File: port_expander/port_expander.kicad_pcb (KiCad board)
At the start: 2 copper layers, 104 x 71 mm, 22 parts, among them J0 Conn_02x08_Male, J1 Conn_02x08_Male, J10 Conn_01x05_Male, J2 Conn_02x08_Male, J3 Conn_02x08_Male, J4 Conn_02x08_Male, J5 Conn_02x08_Male, J6 Conn_02x08_Male, J7 Conn_02x08_Male, J8 Conn_02x08_Male, J9 Conn_02x08_Male, U1 74LS30

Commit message: compact port expander layout
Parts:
- removed H1, H2, H3: MountingHole_3.2mm_M3_Pad, MountingHole:MountingHole_3.2mm_M3_Pad
- removed LOGO: KiCad-Logo2_5mm_SilkScreen, Symbol:KiCad-Logo2_5mm_SilkScreen
- removed OSH: OSHW-Logo2_7.3x6mm_SilkScreen, Symbol:OSHW-Logo2_7.3x6mm_SilkScreen
- added L0: KiCad-Logo_5mm_SilkScreen, Symbol:KiCad-Logo_5mm_SilkScreen, B.Cu at (150.2, 66.9)
- added MH0: MountingHole_3.2mm_M3, MountingHole:MountingHole_3.2mm_M3, F.Cu at (26.5, 59.5)
- added MH1: MountingHole_3.2mm_M3, MountingHole:MountingHole_3.2mm_M3, F.Cu at (150.0, 59.5)
- added MH2: MountingHole_3.2mm_M3, MountingHole:MountingHole_3.2mm_M3, F.Cu at (254.5, 59.5)
- added REF**: OSHW-Logo_5.7x6mm_SilkScreen, Symbol:OSHW-Logo_5.7x6mm_SilkScreen, B.Cu at (240.7, 68.7)
- J0, J1, J2, J3, J4, J5, J6, J7, J8, J9: footprint Connector_PinHeader_2.54mm:PinHeader_2x08_P2.54mm_Vertical -> Connector_PinHeader_2.54mm:PinHeader_2x08_P2.54mm_Horizontal
- U1: value 74LS30 -> 74HC32
- moved PE4 99.6 mm to (228.0, 55.6), turned to 270 degrees
- moved PE3 97.1 mm to (190.5, 55.6), turned to 270 degrees
- moved J9 89.6 mm to (236.5, 71.8), turned to 270 degrees
- moved U1 88.6 mm to (248.0, 55.6), turned to 270 degrees
- moved J1 85.5 mm to (64.3, 71.8), turned to 270 degrees
- moved J7 80.8 mm to (193.4, 71.8), turned to 270 degrees
- moved J0 76.4 mm to (42.8, 71.8), turned to 270 degrees
- moved J8 75.9 mm to (215.0, 71.8), turned to 270 degrees
- moved J3 75.2 mm to (107.3, 71.8), turned to 270 degrees
- moved J6 73.0 mm to (171.9, 71.8), turned to 270 degrees
- moved PE0 67.8 mm to (66.5, 55.6), turned to 270 degrees
- moved J2 65.4 mm to (85.8, 71.8), turned to 270 degrees
- moved J5 65.3 mm to (150.4, 71.8), turned to 270 degrees
- moved PE1 62.3 mm to (104.5, 55.6), turned to 270 degrees
- moved PE2 57.0 mm to (142.5, 55.6), turned to 270 degrees
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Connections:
- J0 pad 1: GND -> /E0B0
- J0 pad 10: Net-(J0-Pad10) -> GND
- J0 pad 11: GND -> /E0B5
- J0 pad 12: Net-(J0-Pad12) -> GND
- J0 pad 13: GND -> /E0B6
- J0 pad 14: Net-(J0-Pad14) -> GND
- J0 pad 15: GND -> /E0B7
- J0 pad 16: Net-(J0-Pad16) -> GND
- J0 pad 2: Net-(J0-Pad2) -> GND
- J0 pad 3: GND -> /E0B1
- J0 pad 4: Net-(J0-Pad4) -> GND
- J0 pad 5: GND -> /E0B2
- J0 pad 6: Net-(J0-Pad6) -> GND
- J0 pad 7: GND -> /E0B3
- J0 pad 8: Net-(J0-Pad8) -> GND
- J0 pad 9: GND -> /E0B4
- J1 pad 1: GND -> /E0A7
- J1 pad 10: Net-(J1-Pad10) -> GND
- J1 pad 11: GND -> /E0A2
- J1 pad 12: Net-(J1-Pad12) -> GND
- J1 pad 13: GND -> /E0A1
- J1 pad 14: Net-(J1-Pad14) -> GND
- J1 pad 15: GND -> /E0A0
- J1 pad 16: Net-(J1-Pad16) -> GND
- J1 pad 2: Net-(J1-Pad2) -> GND
- J1 pad 3: GND -> /E0A6
- J1 pad 4: Net-(J1-Pad4) -> GND
- J1 pad 5: GND -> /E0A5
- J1 pad 6: Net-(J1-Pad6) -> GND
- J1 pad 7: GND -> /E0A4
- J1 pad 8: Net-(J1-Pad8) -> GND
- J1 pad 9: GND -> /E0A3
- J2 pad 1: GND -> /E1B0
- J2 pad 10: Net-(J2-Pad10) -> GND
- J2 pad 11: GND -> /E1B5
- J2 pad 12: Net-(J2-Pad12) -> GND
- J2 pad 13: GND -> /E1B6
- J2 pad 14: Net-(J2-Pad14) -> GND
- J2 pad 15: GND -> /E1B7
- J2 pad 16: Net-(J2-Pad16) -> GND
- J2 pad 2: Net-(J2-Pad2) -> GND
- J2 pad 3: GND -> /E1B1
- J2 pad 4: Net-(J2-Pad4) -> GND
- J2 pad 5: GND -> /E1B2
- J2 pad 6: Net-(J2-Pad6) -> GND
- J2 pad 7: GND -> /E1B3
- J2 pad 8: Net-(J2-Pad8) -> GND
- J2 pad 9: GND -> /E1B4
- J3 pad 1: GND -> /E1A7
- J3 pad 10: Net-(J3-Pad10) -> GND
- J3 pad 11: GND -> /E1A2
- J3 pad 12: Net-(J3-Pad12) -> GND
- J3 pad 13: GND -> /E1A1
- J3 pad 14: Net-(J3-Pad14) -> GND
- J3 pad 15: GND -> /E1A0
- J3 pad 16: Net-(J3-Pad16) -> GND
- J3 pad 2: Net-(J3-Pad2) -> GND
- J3 pad 3: GND -> /E1A6
- J3 pad 4: Net-(J3-Pad4) -> GND
- J3 pad 5: GND -> /E1A5
- J3 pad 6: Net-(J3-Pad6) -> GND
- J3 pad 7: GND -> /E1A4
- J3 pad 8: Net-(J3-Pad8) -> GND
- J3 pad 9: GND -> /E1A3
- J4 pad 1: GND -> /E2B0
- J4 pad 10: Net-(J4-Pad10) -> GND
- J4 pad 11: GND -> /E2B5
- J4 pad 12: Net-(J4-Pad12) -> GND
- J4 pad 13: GND -> /E2B6
- J4 pad 14: Net-(J4-Pad14) -> GND
- J4 pad 15: GND -> /E2B7
- J4 pad 16: Net-(J4-Pad16) -> GND
- J4 pad 2: Net-(J4-Pad2) -> GND
- J4 pad 3: GND -> /E2B1
- J4 pad 4: Net-(J4-Pad4) -> GND
- J4 pad 5: GND -> /E2B2
- J4 pad 6: Net-(J4-Pad6) -> GND
- J4 pad 7: GND -> /E2B3
- J4 pad 8: Net-(J4-Pad8) -> GND
- J4 pad 9: GND -> /E2B4
- J5 pad 1: GND -> /E2A7
- J5 pad 10: Net-(J5-Pad10) -> GND
- J5 pad 11: GND -> /E2A2
- J5 pad 12: Net-(J5-Pad12) -> GND
- J5 pad 13: GND -> /E2A1
- J5 pad 14: Net-(J5-Pad14) -> GND
- J5 pad 15: GND -> /E2A0
- J5 pad 16: Net-(J5-Pad16) -> GND
- J5 pad 2: Net-(J5-Pad2) -> GND
- J5 pad 3: GND -> /E2A6
- J5 pad 4: Net-(J5-Pad4) -> GND
- J5 pad 5: GND -> /E2A5
- J5 pad 6: Net-(J5-Pad6) -> GND
- J5 pad 7: GND -> /E2A4
- J5 pad 8: Net-(J5-Pad8) -> GND
- J5 pad 9: GND -> /E2A3
- J6 pad 1: GND -> /E3B0
- J6 pad 10: Net-(J6-Pad10) -> GND
- J6 pad 11: GND -> /E3B5
- J6 pad 12: Net-(J6-Pad12) -> GND
- J6 pad 13: GND -> /E3B6
- J6 pad 14: Net-(J6-Pad14) -> GND
- J6 pad 15: GND -> /E3B7
- J6 pad 16: Net-(J6-Pad16) -> GND
- J6 pad 2: Net-(J6-Pad2) -> GND
- J6 pad 3: GND -> /E3B1
- J6 pad 4: Net-(J6-Pad4) -> GND
- J6 pad 5: GND -> /E3B2
- J6 pad 6: Net-(J6-Pad6) -> GND
- J6 pad 7: GND -> /E3B3
- J6 pad 8: Net-(J6-Pad8) -> GND
- J6 pad 9: GND -> /E3B4
- J7 pad 1: GND -> /E3A7
- J7 pad 10: Net-(J7-Pad10) -> GND
- J7 pad 11: GND -> /E3A2
- J7 pad 12: Net-(J7-Pad12) -> GND
- J7 pad 13: GND -> /E3A1
- J7 pad 14: Net-(J7-Pad14) -> GND
- J7 pad 15: GND -> /E3A0
- J7 pad 16: Net-(J7-Pad16) -> GND
- J7 pad 2: Net-(J7-Pad2) -> GND
- J7 pad 3: GND -> /E3A6
- J7 pad 4: Net-(J7-Pad4) -> GND
- J7 pad 5: GND -> /E3A5
- J7 pad 6: Net-(J7-Pad6) -> GND
- J7 pad 7: GND -> /E3A4
- J7 pad 8: Net-(J7-Pad8) -> GND
- J7 pad 9: GND -> /E3A3
- J8 pad 1: GND -> /E4B0
- J8 pad 10: Net-(J8-Pad10) -> GND
- J8 pad 11: GND -> /E4B5
- J8 pad 12: Net-(J8-Pad12) -> GND
- J8 pad 13: GND -> /E4B6
- J8 pad 14: Net-(J8-Pad14) -> GND
- J8 pad 15: GND -> /E4B7
- J8 pad 16: Net-(J8-Pad16) -> GND
- J8 pad 2: Net-(J8-Pad2) -> GND
- J8 pad 3: GND -> /E4B1
- J8 pad 4: Net-(J8-Pad4) -> GND
- J8 pad 5: GND -> /E4B2
- J8 pad 6: Net-(J8-Pad6) -> GND
- J8 pad 7: GND -> /E4B3
- J8 pad 8: Net-(J8-Pad8) -> GND
- J8 pad 9: GND -> /E4B4
- J9 pad 1: GND -> /E4A7
- J9 pad 10: Net-(J9-Pad10) -> GND
- J9 pad 11: GND -> /E4A2
- J9 pad 12: Net-(J9-Pad12) -> GND
- J9 pad 13: GND -> /E4A1
- J9 pad 14: Net-(J9-Pad14) -> GND
- J9 pad 15: GND -> /E4A0
- J9 pad 16: Net-(J9-Pad16) -> GND
- J9 pad 2: Net-(J9-Pad2) -> GND
- J9 pad 3: GND -> /E4A6
- J9 pad 4: Net-(J9-Pad4) -> GND
- J9 pad 5: GND -> /E4A5
- J9 pad 6: Net-(J9-Pad6) -> GND
- J9 pad 7: GND -> /E4A4
- J9 pad 8: Net-(J9-Pad8) -> GND
- J9 pad 9: GND -> /E4A3
- PE0 pad 1: Net-(J0-Pad2) -> /E0B0
- PE0 pad 2: Net-(J0-Pad4) -> /E0B1
- PE0 pad 21: Net-(J1-Pad2) -> /E0A0
- PE0 pad 22: Net-(J1-Pad4) -> /E0A1
- PE0 pad 23: Net-(J1-Pad6) -> /E0A2
- PE0 pad 24: Net-(J1-Pad8) -> /E0A3
- PE0 pad 25: Net-(J1-Pad10) -> /E0A4
- PE0 pad 26: Net-(J1-Pad12) -> /E0A5
- PE0 pad 27: Net-(J1-Pad14) -> /E0A6
- PE0 pad 28: Net-(J1-Pad16) -> /E0A7
- PE0 pad 3: Net-(J0-Pad6) -> /E0B2
- PE0 pad 4: Net-(J0-Pad8) -> /E0B3
- PE0 pad 5: Net-(J0-Pad10) -> /E0B4
- PE0 pad 6: Net-(J0-Pad12) -> /E0B5
- PE0 pad 7: Net-(J0-Pad14) -> /E0B6
- PE0 pad 8: Net-(J0-Pad16) -> /E0B7
- PE1 pad 1: Net-(J2-Pad2) -> /E1B0
- PE1 pad 2: Net-(J2-Pad4) -> /E1B1
- PE1 pad 21: Net-(J3-Pad2) -> /E1A0
- PE1 pad 22: Net-(J3-Pad4) -> /E1A1
- PE1 pad 23: Net-(J3-Pad6) -> /E1A2
- PE1 pad 24: Net-(J3-Pad8) -> /E1A3
- PE1 pad 25: Net-(J3-Pad10) -> /E1A4
- PE1 pad 26: Net-(J3-Pad12) -> /E1A5
- PE1 pad 27: Net-(J3-Pad14) -> /E1A6
- PE1 pad 28: Net-(J3-Pad16) -> /E1A7
- PE1 pad 3: Net-(J2-Pad6) -> /E1B2
- PE1 pad 4: Net-(J2-Pad8) -> /E1B3
- PE1 pad 5: Net-(J2-Pad10) -> /E1B4
- PE1 pad 6: Net-(J2-Pad12) -> /E1B5
- PE1 pad 7: Net-(J2-Pad14) -> /E1B6
- PE1 pad 8: Net-(J2-Pad16) -> /E1B7
- PE2 pad 1: Net-(J4-Pad2) -> /E2B0
- PE2 pad 2: Net-(J4-Pad4) -> /E2B1
- PE2 pad 21: Net-(J5-Pad2) -> /E2A0
- PE2 pad 22: Net-(J5-Pad4) -> /E2A1
- PE2 pad 23: Net-(J5-Pad6) -> /E2A2
- PE2 pad 24: Net-(J5-Pad8) -> /E2A3
- PE2 pad 25: Net-(J5-Pad10) -> /E2A4
- PE2 pad 26: Net-(J5-Pad12) -> /E2A5
- PE2 pad 27: Net-(J5-Pad14) -> /E2A6
- PE2 pad 28: Net-(J5-Pad16) -> /E2A7
- PE2 pad 3: Net-(J4-Pad6) -> /E2B2
- PE2 pad 4: Net-(J4-Pad8) -> /E2B3
- PE2 pad 5: Net-(J4-Pad10) -> /E2B4
- PE2 pad 6: Net-(J4-Pad12) -> /E2B5
- PE2 pad 7: Net-(J4-Pad14) -> /E2B6
- PE2 pad 8: Net-(J4-Pad16) -> /E2B7
- PE3 pad 1: Net-(J6-Pad2) -> /E3B0
- PE3 pad 2: Net-(J6-Pad4) -> /E3B1
- PE3 pad 21: Net-(J7-Pad2) -> /E3A0
- PE3 pad 22: Net-(J7-Pad4) -> /E3A1
- PE3 pad 23: Net-(J7-Pad6) -> /E3A2
- PE3 pad 24: Net-(J7-Pad8) -> /E3A3
- PE3 pad 25: Net-(J7-Pad10) -> /E3A4
- PE3 pad 26: Net-(J7-Pad12) -> /E3A5
- PE3 pad 27: Net-(J7-Pad14) -> /E3A6
- PE3 pad 28: Net-(J7-Pad16) -> /E3A7
- PE3 pad 3: Net-(J6-Pad6) -> /E3B2
- PE3 pad 4: Net-(J6-Pad8) -> /E3B3
- PE3 pad 5: Net-(J6-Pad10) -> /E3B4
- PE3 pad 6: Net-(J6-Pad12) -> /E3B5
- PE3 pad 7: Net-(J6-Pad14) -> /E3B6
- PE3 pad 8: Net-(J6-Pad16) -> /E3B7
- PE4 pad 1: Net-(J8-Pad2) -> /E4B0
- PE4 pad 2: Net-(J8-Pad4) -> /E4B1
- PE4 pad 21: Net-(J9-Pad2) -> /E4A0
- PE4 pad 22: Net-(J9-Pad4) -> /E4A1
- PE4 pad 23: Net-(J9-Pad6) -> /E4A2
- PE4 pad 24: Net-(J9-Pad8) -> /E4A3
- PE4 pad 25: Net-(J9-Pad10) -> /E4A4
- PE4 pad 26: Net-(J9-Pad12) -> /E4A5
- PE4 pad 27: Net-(J9-Pad14) -> /E4A6
- PE4 pad 28: Net-(J9-Pad16) -> /E4A7
- PE4 pad 3: Net-(J8-Pad6) -> /E4B2
- PE4 pad 4: Net-(J8-Pad8) -> /E4B3
- PE4 pad 5: Net-(J8-Pad10) -> /E4B4
- PE4 pad 6: Net-(J8-Pad12) -> /E4B5
- PE4 pad 7: Net-(J8-Pad14) -> /E4B6
- PE4 pad 8: Net-(J8-Pad16) -> /E4B7
- U1 pad 10: (no net) -> /INT3
- U1 pad 11: +3V3 -> /INT
- U1 pad 12: +3V3 -> Net-(U1-Pad12)
- U1 pad 13: (no net) -> /INT4
- U1 pad 3: /INT2 -> Net-(U1-Pad3)
- U1 pad 4: /INT3 -> Net-(U1-Pad3)
- U1 pad 5: /INT4 -> /INT2
- U1 pad 6: +3V3 -> Net-(U1-Pad6)
- U1 pad 8: /INT -> Net-(U1-Pad12)
- U1 pad 9: (no net) -> Net-(U1-Pad6)
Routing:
- net /SCK: track 99.2 -> 232.6 mm
- net /INT1: track 43.7 -> 175.6 mm
- net /INT0: track 75.9 -> 207.7 mm
- net /SDA: track 107.0 -> 235.3 mm
- net +3V3: track 179.5 -> 281.6 mm
- net /INT2: track 27.1 -> 122.0 mm
- net /E3B1: track 0.00 -> 89.5 mm
- net /E3B2: track 0.00 -> 55.6 mm
- net /E0B1: track 0.00 -> 47.9 mm
- net /E3B0: track 0.00 -> 47.9 mm
- net /E0B2: track 0.00 -> 44.3 mm
- net /E0B3: track 0.00 -> 41.5 mm
- net /E3B3: track 0.00 -> 37.9 mm
- net /E1B0: track 0.00 -> 36.4 mm
- net /E0B5: track 0.00 -> 35.7 mm
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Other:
- board size 104 x 71 mm -> 239 x 26 mm
- net class Power: clearance 0.4 -> 0.3; trace_width 0.5 -> 0.3; via_dia 1.6 -> 1; via_drill 0.8 -> 0.5
- board text added: "Port Expander 80 GPIOs I2C"
- board text removed: "Port Expander Interrupt 80 GPIOs I2C"

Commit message: port expander with MCU
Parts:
- added J11: Power_Jack, Connector_PinHeader_2.54mm:PinHeader_1x02_P2.54mm_Vertical, F.Cu at (296.0, 49.0)
- added MC1: ESP32_DevKitC, esp32_driver:ESP32_DevKitC, F.Cu at (345.0, 79.2)
- J10: value Conn_01x05_Male -> OLED_Display; footprint Connector_PinHeader_2.54mm:PinHeader_1x05_P2.54mm_Vertical -> Connector_PinHeader_2.54mm:PinHeader_1x04_P2.54mm_Vertical
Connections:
- J10 pad 3: /SDA -> /SCK
- J10 pad 4: /SCK -> /SDA
- PE0 pad 11: (no net) -> Net-(PE0-Pad11)
- PE0 pad 14: (no net) -> Net-(PE0-Pad14)
- PE0 pad 19: (no net) -> Net-(PE0-Pad19)
- PE1 pad 11: (no net) -> Net-(PE1-Pad11)
- PE1 pad 14: (no net) -> Net-(PE1-Pad14)
- PE1 pad 19: (no net) -> Net-(PE1-Pad19)
- PE2 pad 11: (no net) -> Net-(PE2-Pad11)
- PE2 pad 14: (no net) -> Net-(PE2-Pad14)
- PE2 pad 19: (no net) -> Net-(PE2-Pad19)
- PE3 pad 11: (no net) -> Net-(PE3-Pad11)
- PE3 pad 14: (no net) -> Net-(PE3-Pad14)
- PE3 pad 19: (no net) -> Net-(PE3-Pad19)
- PE4 pad 11: (no net) -> Net-(PE4-Pad11)
- PE4 pad 14: (no net) -> Net-(PE4-Pad14)
- PE4 pad 19: (no net) -> Net-(PE4-Pad19)
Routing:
- net GND: track 392.6 -> 0.00 mm
- net +3V3: track 281.6 -> 0.00 mm
- net /SDA: track 235.3 -> 0.00 mm
- net /SCK: track 232.6 -> 0.00 mm
- net /INT0: track 207.7 -> 0.00 mm
- net /INT1: track 175.6 -> 0.00 mm
- net /INT2: track 122.0 -> 0.00 mm
- net /E3B1: track 89.5 -> 0.00 mm
- net /INT3: track 69.3 -> 0.00 mm
- net /E3B2: track 55.6 -> 0.00 mm
- net /E0B1: track 47.9 -> 0.00 mm
- net /E3B0: track 47.9 -> 0.00 mm
- net /E0B2: track 44.3 -> 0.00 mm
- net /E0B3: track 41.5 -> 0.00 mm
- net /INT4: track 40.4 -> 0.00 mm
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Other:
- board text removed: "INT"

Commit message: complete main board
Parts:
- added BZ1: Buzzer, esp32_driver:PassiveBuzzer_D12_H8.2_P6.6, F.Cu at (271.0, 122.0)
- added J12: SD, Connector_PinHeader_2.54mm:PinHeader_1x06_P2.54mm_Vertical, F.Cu at (257.1, 117.4)
- added J13: Dial, Connector_PinHeader_2.54mm:PinHeader_1x05_P2.54mm_Vertical, F.Cu at (261.8, 117.4)
- added Q1: BC548, Package_TO_SOT_THT:TO-92_Inline, F.Cu at (288.3, 122.4)
- added R1: 680, Resistor_THT:R_Axial_DIN0207_L6.3mm_D2.5mm_P10.16mm_Horizontal, F.Cu at (256.4, 134.5)
- added R2: 150, Resistor_THT:R_Axial_DIN0207_L6.3mm_D2.5mm_P10.16mm_Horizontal, F.Cu at (279.5, 117.1)
- added R3: 150, Resistor_THT:R_Axial_DIN0207_L6.3mm_D2.5mm_P10.16mm_Horizontal, F.Cu at (269.7, 130.9)
- added RV1: 10K, esp32_driver:BOURNS-3362P_pot, F.Cu at (282.1, 123.3)
- J10: value OLED_Display -> Display
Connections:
- J8 pad 10: GND -> Net-(J8-Pad10)
- J8 pad 12: GND -> Net-(J8-Pad10)
- J8 pad 14: GND -> Net-(J8-Pad10)
- J8 pad 16: GND -> Net-(J8-Pad10)
- J8 pad 2: GND -> Net-(J8-Pad10)
- J8 pad 4: GND -> Net-(J8-Pad10)
- J8 pad 6: GND -> Net-(J8-Pad10)
- J8 pad 8: GND -> Net-(J8-Pad10)
- J9 pad 10: GND -> Net-(J9-Pad10)
- J9 pad 12: GND -> Net-(J9-Pad10)
- J9 pad 14: GND -> Net-(J9-Pad10)
- J9 pad 16: GND -> Net-(J9-Pad10)
- J9 pad 2: GND -> Net-(J9-Pad10)
- J9 pad 4: GND -> Net-(J9-Pad10)
- J9 pad 6: GND -> Net-(J9-Pad10)
- J9 pad 8: GND -> Net-(J9-Pad10)
- MC1 pad 10: Net-(MC1-Pad10) -> /RTB
- MC1 pad 11: Net-(MC1-Pad11) -> /RTA
- MC1 pad 13: Net-(MC1-Pad13) -> /BUZ
- MC1 pad 21: Net-(MC1-Pad21) -> /MOSI
- MC1 pad 27: Net-(MC1-Pad27) -> /MISO
- MC1 pad 28: Net-(MC1-Pad28) -> /SPICLK
- MC1 pad 29: Net-(MC1-Pad29) -> /SPICS
- MC1 pad 9: Net-(MC1-Pad9) -> /RTS
- PE4 pad 20: /INT4 -> Net-(PE4-Pad20)
- U1 pad 13: /INT4 -> GND
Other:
- net class Power: clearance 0.3 -> 0.2

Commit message: main board routing
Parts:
- removed MH0: MountingHole_3.2mm_M3, MountingHole:MountingHole_3.2mm_M3
- added MH3: MountingHole_3.2mm_M3, MountingHole:MountingHole_3.2mm_M3, F.Cu at (166.0, 147.0)
- added MH4: MountingHole_3.2mm_M3, MountingHole:MountingHole_3.2mm_M3, F.Cu at (66.0, 147.0)
- moved MC1 277.2 mm to (76.0, 146.0), turned to 0 degrees
- moved J11 244.3 mm to (67.0, 134.0), turned to 0 degrees
- moved RV1 207.1 mm to (78.0, 88.0), turned to 270 degrees
- moved Q1 202.4 mm to (92.0, 73.0), turned to 90 degrees
- moved J13 195.8 mm to (67.0, 97.0)
- moved J12 194.8 mm to (67.0, 75.0)
- moved R1 191.2 mm to (76.0, 71.0), turned to 270 degrees
- moved J10 183.5 mm to (67.0, 117.0), turned to 0 degrees
- moved BZ1 182.8 mm to (92.0, 85.0), turned to 90 degrees
- moved R2 174.1 mm to (107.0, 141.0), turned to 90 degrees
- moved U1 130.9 mm to (128.0, 108.0)
- moved R3 120.0 mm to (150.0, 140.0)
- moved L0 117.5 mm to (266.0, 47.0)
- moved J8 114.3 mm to (127.0, 144.8)
- moved J9 114.3 mm to (148.5, 144.8)
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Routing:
- net GND: track 0.00 -> 402.1 mm
- net +3V3: track 0.00 -> 326.8 mm
- net /SDA: track 0.00 -> 227.3 mm
- net /SCK: track 0.00 -> 224.3 mm
- net /INT1: track 0.00 -> 75.2 mm
- net /SPICLK: track 0.00 -> 62.7 mm
- net /INT3: track 0.00 -> 62.1 mm
- net /SPICS: track 0.00 -> 61.1 mm
- net /MISO: track 0.00 -> 58.6 mm
- net /INT0: track 0.00 -> 56.1 mm
- net /INT2: track 0.00 -> 45.9 mm
- net /INT: track 0.00 -> 45.6 mm
- net /MOSI: track 0.00 -> 42.8 mm
- net /E0B3: track 0.00 -> 42.6 mm
- net /E0B4: track 0.00 -> 42.5 mm
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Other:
- board size 239 x 26 mm -> 110 x 110 mm

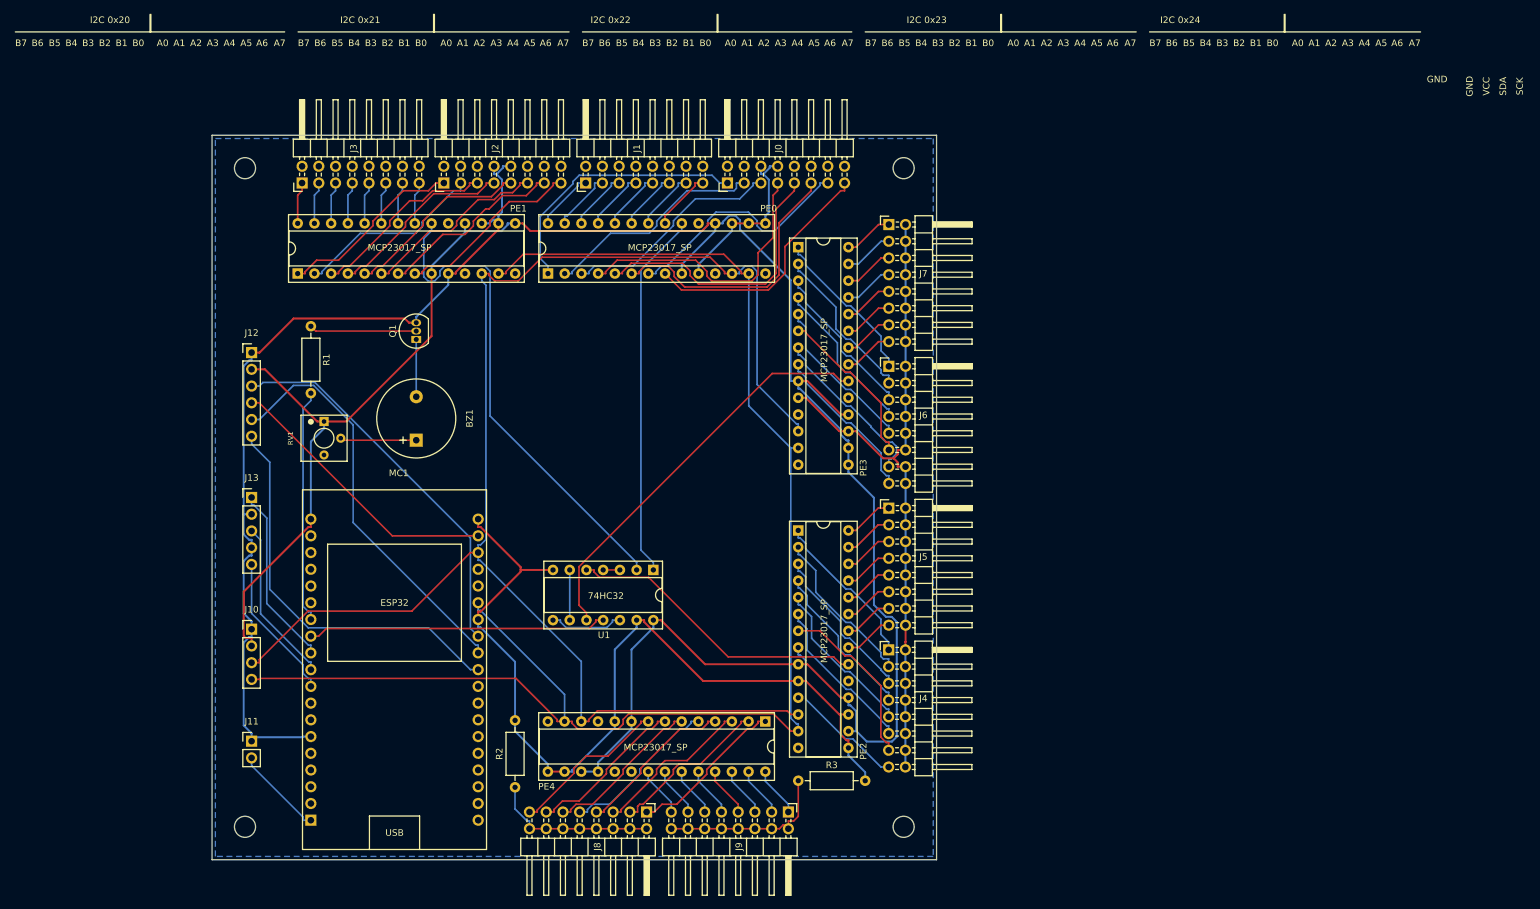
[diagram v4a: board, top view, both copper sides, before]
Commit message: refined routing
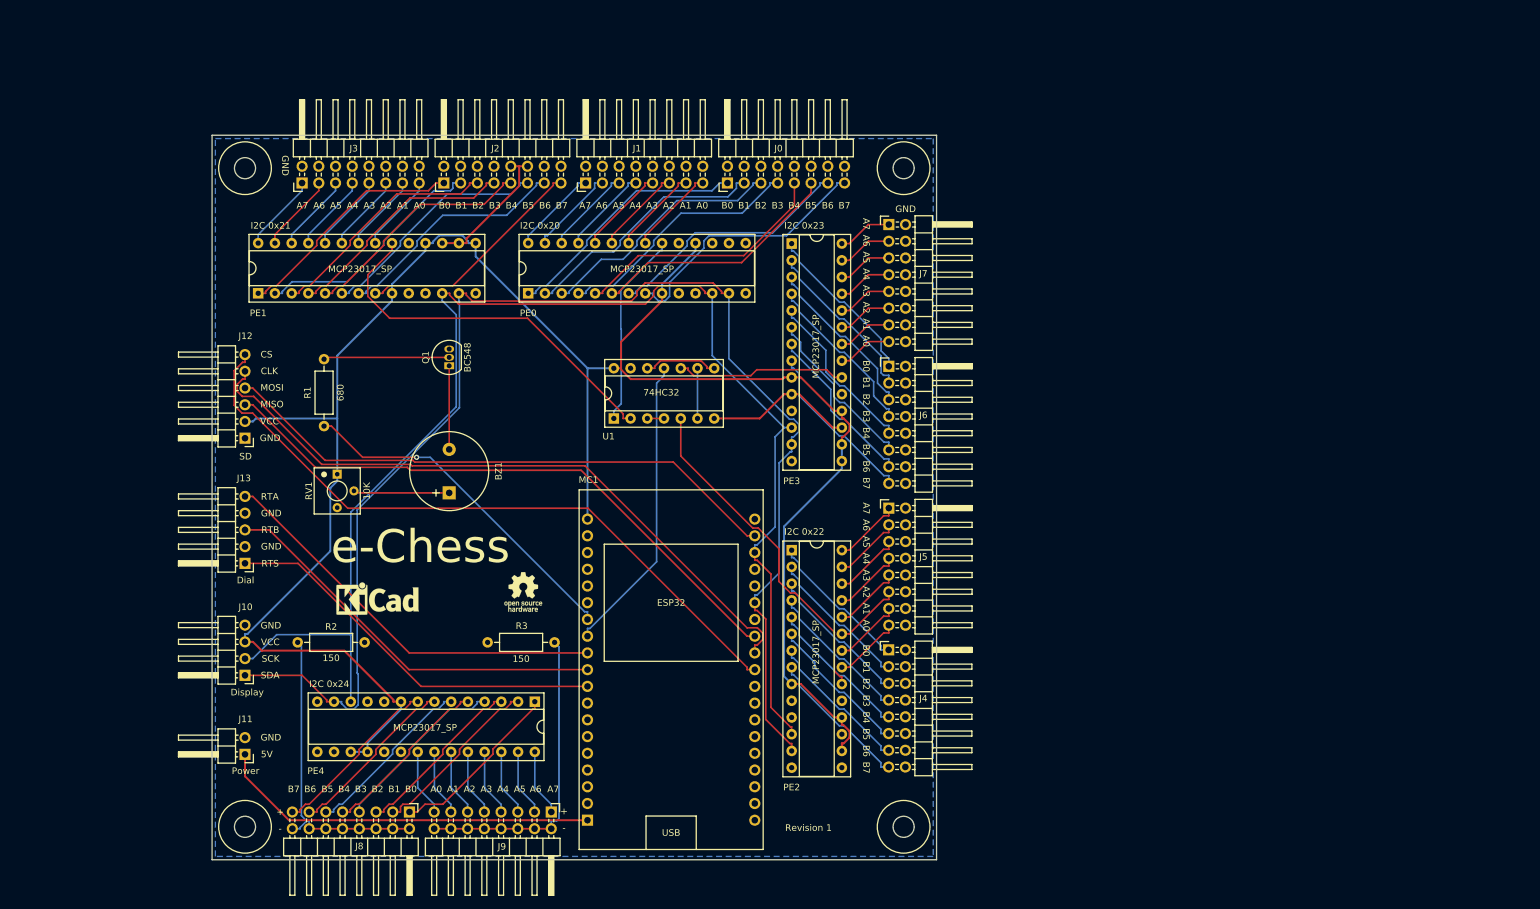
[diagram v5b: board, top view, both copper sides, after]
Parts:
- J10: footprint Connector_PinHeader_2.54mm:PinHeader_1x04_P2.54mm_Vertical -> Connector_PinHeader_2.54mm:PinHeader_1x04_P2.54mm_Horizontal
- J11: value Power_Jack -> Power; footprint Connector_PinHeader_2.54mm:PinHeader_1x02_P2.54mm_Vertical -> Connector_PinHeader_2.54mm:PinHeader_1x02_P2.54mm_Horizontal
- J12: footprint Connector_PinHeader_2.54mm:PinHeader_1x06_P2.54mm_Vertical -> Connector_PinHeader_2.54mm:PinHeader_1x06_P2.54mm_Horizontal
- J13: footprint Connector_PinHeader_2.54mm:PinHeader_1x05_P2.54mm_Vertical -> Connector_PinHeader_2.54mm:PinHeader_1x05_P2.54mm_Horizontal
- L0, REF**: moved to F.Cu
- moved L0 191.5 mm to (86.1, 112.9)
- moved REF** 164.9 mm to (108.2, 111.3)
- moved R3 42.5 mm to (113.0, 119.0), turned to 180 degrees
- moved MC1 42.0 mm to (118.0, 146.0)
- moved R2 39.7 mm to (74.0, 119.0), turned to 0 degrees
- moved J8 36.0 mm to (91.0, 144.8)
- moved J9 36.0 mm to (112.5, 144.8)
- moved PE4 35.1 mm to (110.0, 128.0)
- moved U1 23.8 mm to (122.0, 85.0), turned to 90 degrees
- moved J12 13.0 mm to (66.0, 88.0), turned to 180 degrees
- moved J13 10.0 mm to (66.0, 107.0), turned to 180 degrees
- moved BZ1 9.43 mm to (97.0, 93.0)
- moved RV1 8.25 mm to (80.0, 96.0)
- moved J10 7.07 mm to (66.0, 124.0), turned to 180 degrees
- moved PE1 6.71 mm to (68.0, 66.0)
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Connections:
- J10 pad 1: GND -> /SDA
- J10 pad 2: +3V3 -> /SCK
- J10 pad 3: /SCK -> +3V3
- J10 pad 4: /SDA -> GND
- J11 pad 1: GND -> /5V
- J11 pad 2: Net-(J11-Pad2) -> GND
- J13 pad 1: /RTA -> /RTS
- J13 pad 5: /RTS -> /RTA
- MC1 pad 1: Net-(J11-Pad2) -> /5V
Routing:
- net GND: track 402.1 -> 44.5 mm
- net /5V: track 0.00 -> 58.1 mm
- net /MOSI: track 42.8 -> 86.7 mm
- net /SPICS: track 61.1 -> 104.5 mm
- net /SPICLK: track 62.7 -> 102.5 mm
- net /RTS: track 22.5 -> 59.7 mm
- net /INT3: track 62.1 -> 25.9 mm
- net /RTB: track 25.0 -> 60.8 mm
- net /RTA: track 27.8 -> 61.8 mm
- net /MISO: track 58.6 -> 92.0 mm
- net /INT0: track 56.1 -> 29.9 mm
- net Net-(J8-Pad10): track 25.2 -> 47.2 mm
- net Net-(J9-Pad10): track 26.4 -> 47.3 mm
- net /INT1: track 75.2 -> 57.6 mm
- net /BUZ: track 35.6 -> 52.8 mm, vias 0 -> 1
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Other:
- board text added: "+"
- board text added: "-"
- board text added: "5V"
- board text added: "CLK"
- board text added: "CS"
- board text added: "MISO"
- board text added: "MOSI"
- board text added: "RTA"
- board text added: "RTB"
- board text added: "RTS"
- board text added: "Revision 1"
- board text added: "e-Chess"
- board text removed: "Emmanuel Bastien"
- board text removed: "Port Expander 80 GPIOs I2C"

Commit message: pcb manufacturing
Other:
- board text added: "JLCJLCJLCJLC"
